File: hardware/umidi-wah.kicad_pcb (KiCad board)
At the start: 2 copper layers, 86 parts, among them J1 Conn_01x02, J10 Conn_02x05_Odd_Even, J11 Pots Main, J12 Pots Front, J2 Conn_01x02, J3 Conn_02x05_Odd_Even, J4 Conn_01x02, J5 Input, J6 Output, J7 Conn_02x05_Odd_Even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

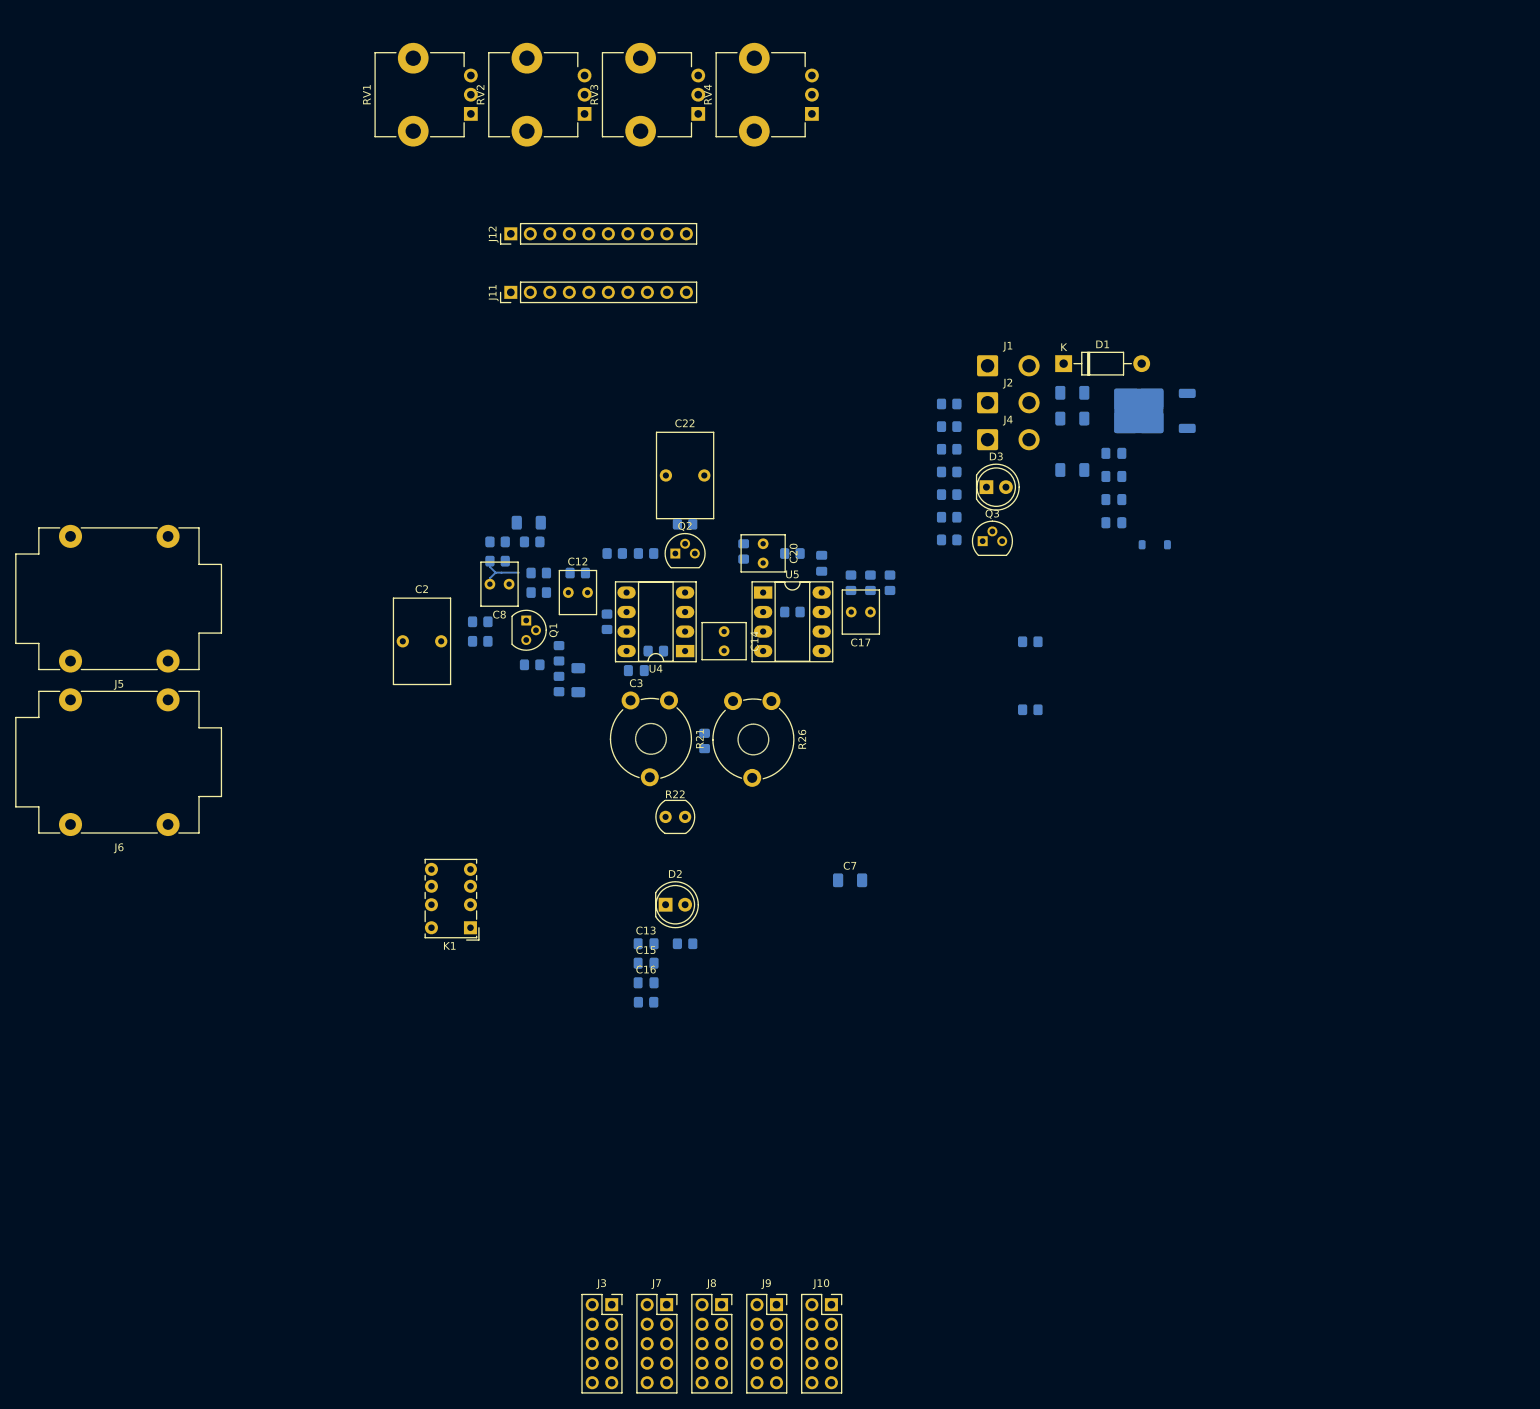
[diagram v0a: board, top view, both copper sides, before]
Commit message: Add pcb outline and test milling layer
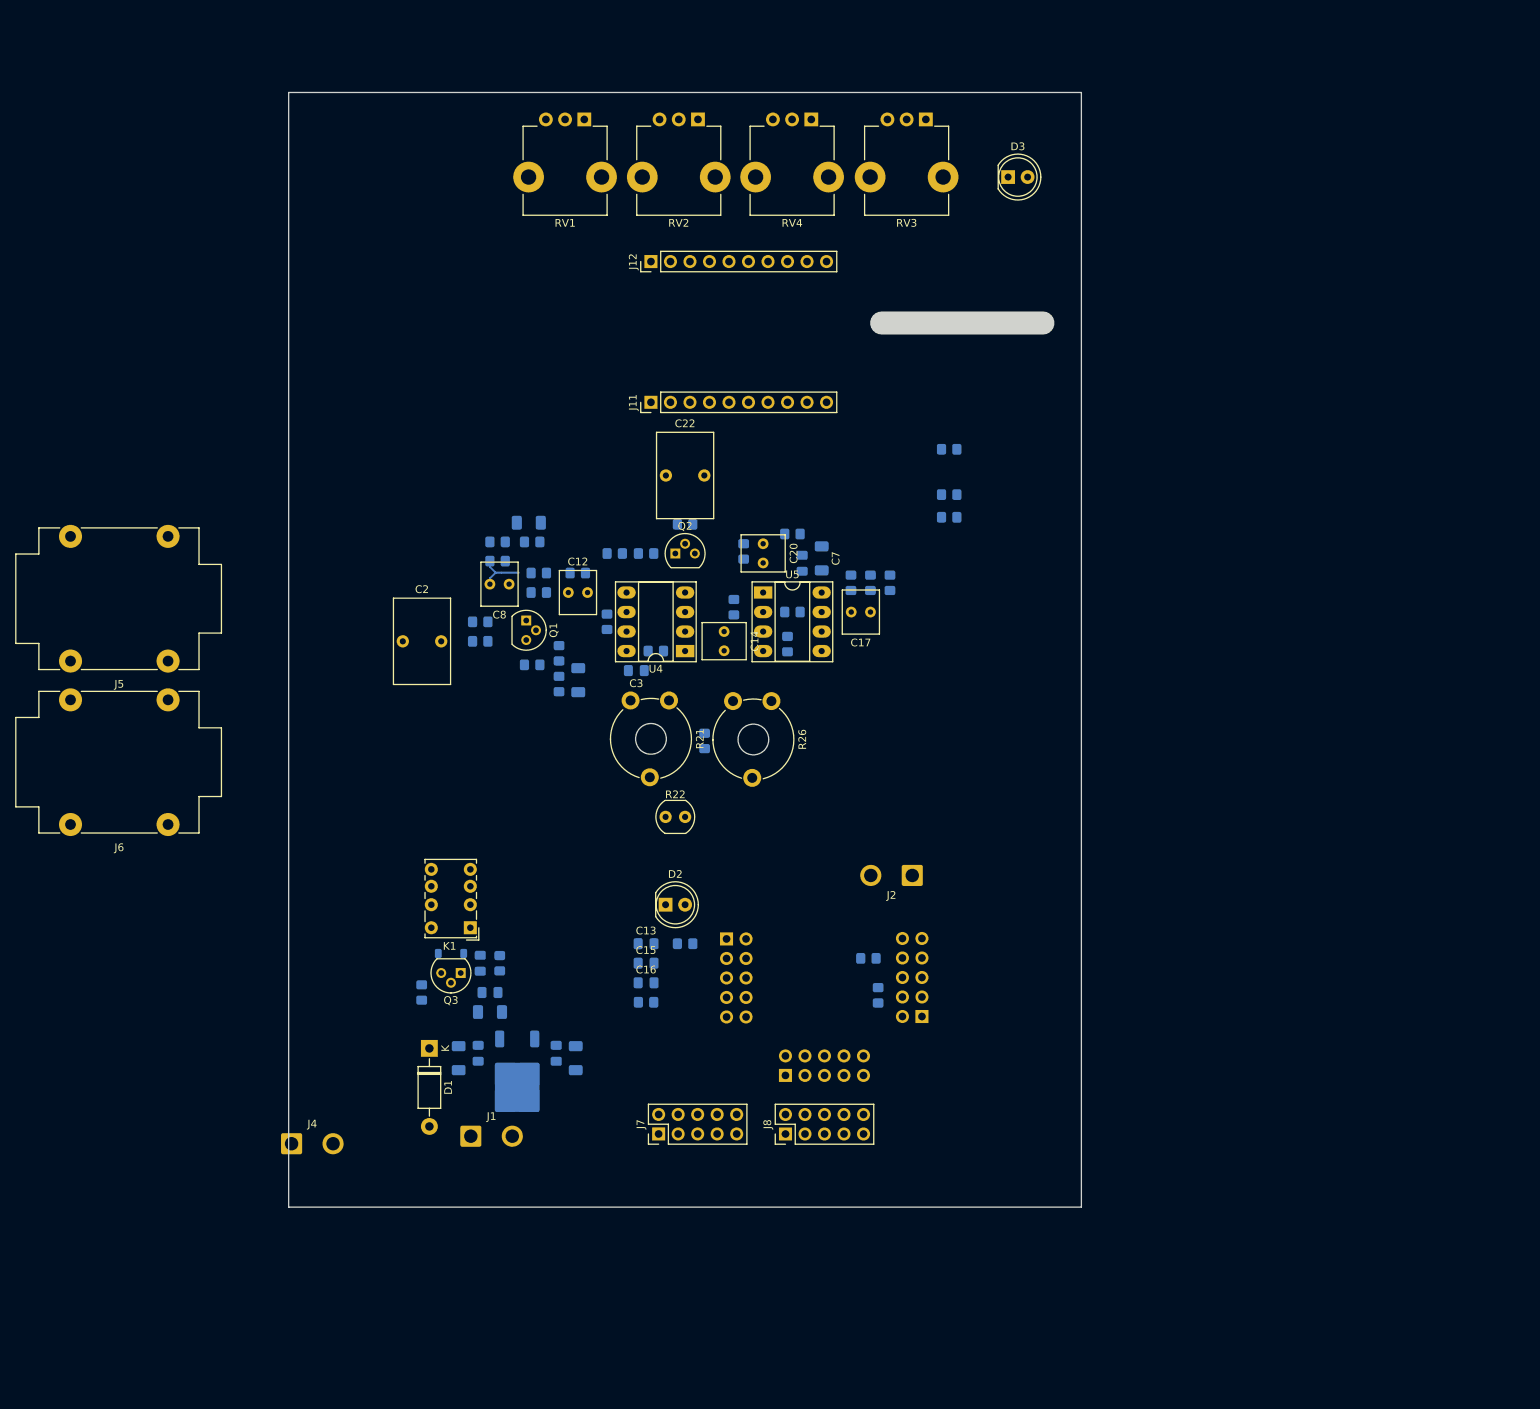
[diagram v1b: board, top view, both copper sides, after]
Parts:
- J10, J3, J9: moved to B.Cu
- J7, J8: footprint Connector_PinSocket_2.54mm:PinSocket_2x05_P2.54mm_Vertical -> Connector_PinHeader_2.54mm:PinHeader_2x05_P2.54mm_Vertical
- moved J4 128.9 mm to (54.2, 156.8)
- moved D1 121.5 mm to (72.1, 144.4), turned to -90 degrees
- moved J1 120.8 mm to (77.5, 155.9)
- moved U3 119.5 mm to (83.5, 148.2), turned to -90 degrees
- moved C4 117.8 mm to (75.9, 145.7), turned to -90 degrees
- moved C5 113.8 mm to (78.5, 145.1), turned to -90 degrees
- moved D4 106.0 mm to (74.9, 132.1)
- moved C10 105.4 mm to (91.2, 145.7), turned to -90 degrees
- moved C9 104.4 mm to (88.6, 145.1), turned to -90 degrees
- moved C18 103.6 mm to (80.0, 139.7)
- moved C19 103.5 mm to (80.0, 137.2)
- moved C21 100.5 mm to (78.7, 133.3), turned to -90 degrees
- moved R35 90.5 mm to (71.1, 137.2), turned to -90 degrees
- moved Q3 88.2 mm to (76.2, 134.6), turned to 180 degrees
- moved R29 86.7 mm to (81.3, 133.3), turned to -90 degrees
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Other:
- board outline added: 103.2 x 145.1 mm

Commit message: Compact parts
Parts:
- moved J4 129.4 mm to (166.4, 92.4), turned to -90 degrees
- moved J6 122.6 mm to (160.7, 112.9), turned to -90 degrees
- moved J5 103.1 mm to (139.4, 112.9), turned to -90 degrees
- moved J1 100.4 mm to (166.4, 109.2), turned to 90 degrees
- moved R31 82.1 mm to (82.1, 130.8), turned to 0 degrees
- moved R28 78.3 mm to (82.1, 119.4), turned to -90 degrees
- moved R32 76.2 mm to (87.6, 130.8)
- moved J10 62.6 mm to (149.9, 93.8)
- moved J8 62.6 mm to (149.9, 101.4)
- moved R24 62.6 mm to (160.7, 78.6)
- moved R25 62.6 mm to (162.0, 83.4)
- moved J3 62.6 mm to (167.7, 86.1)
- moved J9 62.6 mm to (142.2, 76.0)
- moved J7 62.6 mm to (133.4, 101.4)
- moved J2 62.6 mm to (166.4, 67.8)
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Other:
- board size 103.2 x 145.1 mm -> 100.7 x 113.4 mm

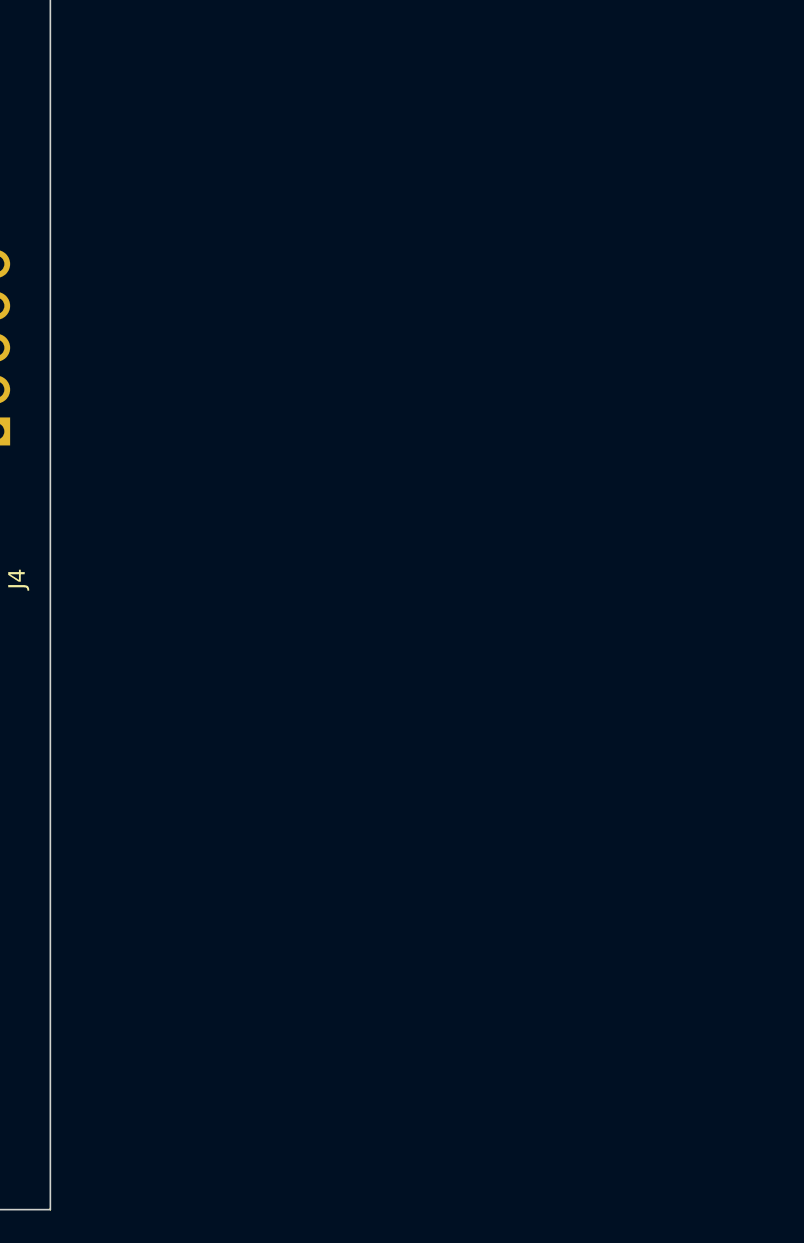
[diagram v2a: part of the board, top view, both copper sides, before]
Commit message: Add uMIDI footprint
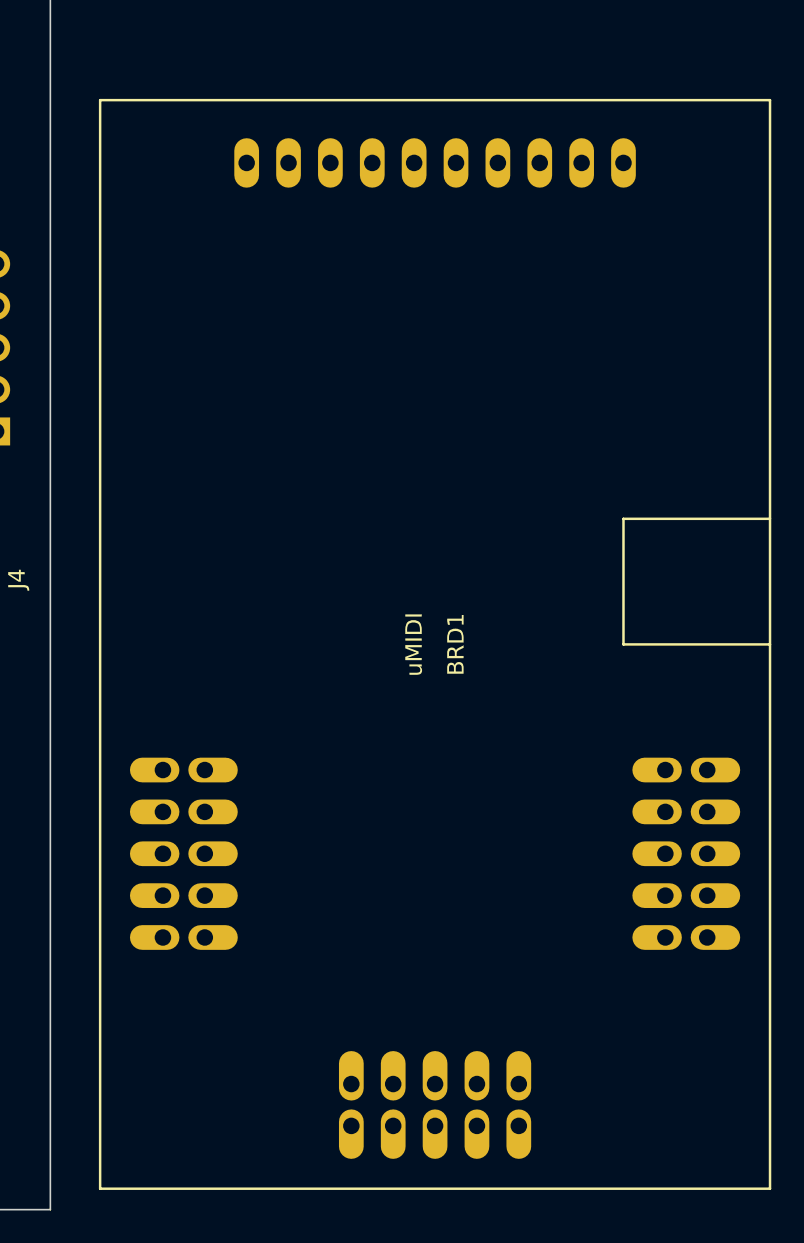
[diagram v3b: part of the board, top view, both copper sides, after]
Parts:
- added BRD1: uMIDI, uMidi-wah:uMIDI_faceup, F.Cu at (194.3, 99.1)
